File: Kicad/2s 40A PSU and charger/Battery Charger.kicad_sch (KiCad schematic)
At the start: 42 parts

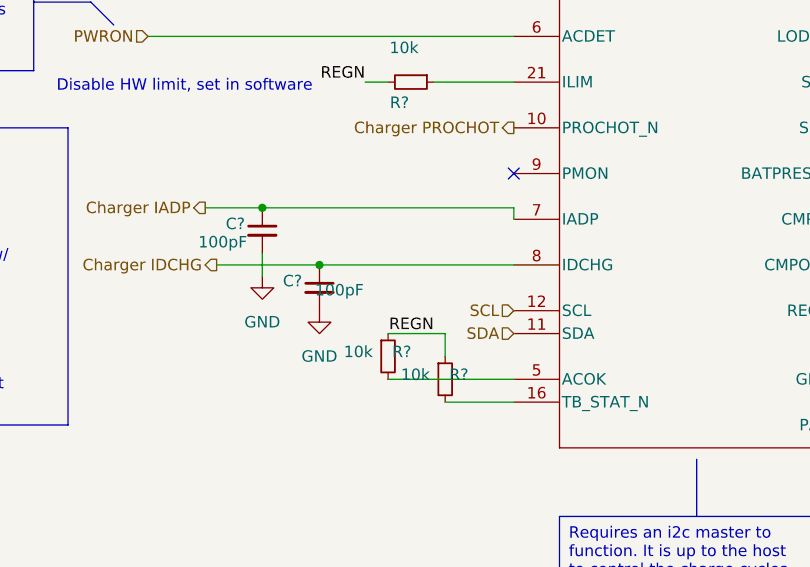
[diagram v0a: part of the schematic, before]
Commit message: Disconnect REGN from unneeded output pullups
These pullups will instead be pulled to 3v3, which should be closer locally. I don't use them but pullups are required for internal detection.
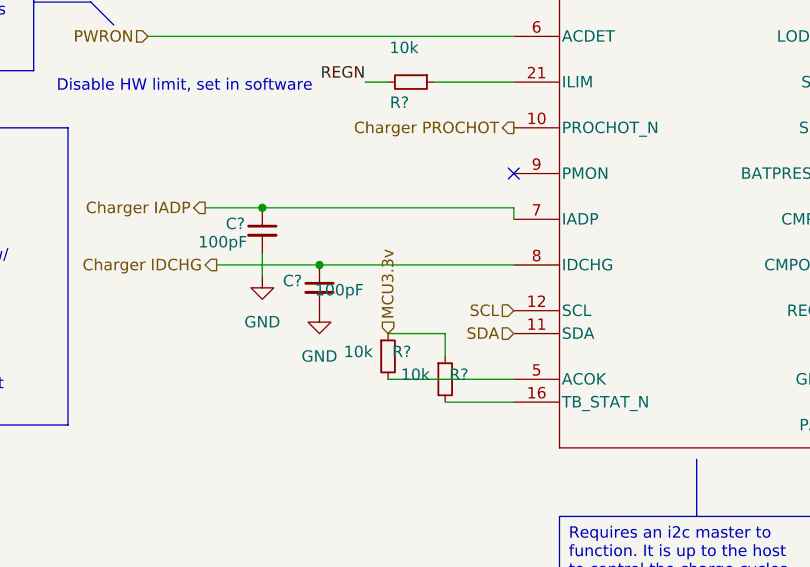
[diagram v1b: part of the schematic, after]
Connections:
- net REGN: no longer R?.1, R?.1
- new net MCU3.3v: R?.1, R?.1
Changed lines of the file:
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@@
-	)
-	(label "REGN"
-		(at 102.87 146.05 180)
-		(fields_autoplaced yes)
-		(effects
-			(font
-				(size 1.27 1.27)
-			)
-			(justify right bottom)
-		)
-		(property "Netclass" "Logic Pwr"
-			(at 102.87 147.32 0)
-			(effects
-				(font
-					(size 1.27 1.27)
-					(italic yes)
-				)
-				(justify right)
-			)
-		)
 	)
 	(label "REGN"
@@
 			(effects
 				(font
+					(size 1.27 1.27)
+					(italic yes)
+				)
+				(justify left)
+			)
+		)
+	)
+	(hierarchical_label "MCU3.3v"
+		(shape input)
+		(at 97.79 146.05 90)
+		(fields_autoplaced yes)
+		(effects
+			(font
+				(size 1.27 1.27)
+			)
+			(justify left)
+		)
+		(property "Netclass" "Logic Pwr"
+			(at 99.06 146.05 90)
+			(effects
+				(font

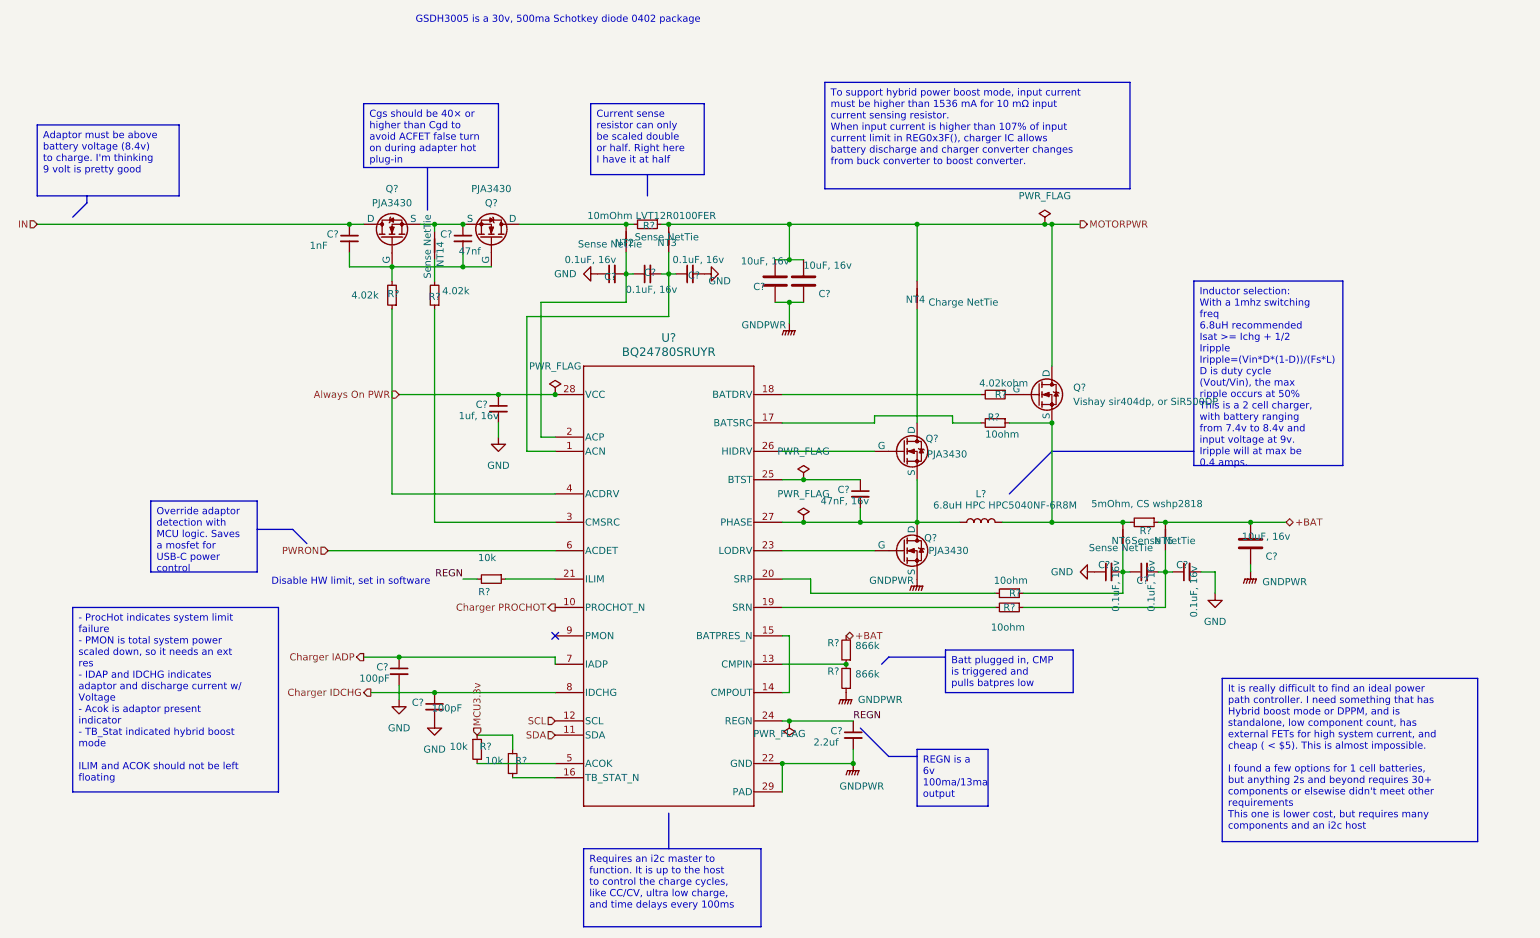
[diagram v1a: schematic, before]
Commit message: Combined separate ground planes
I now have one solid ground plane. There really was no point in having separate ground planes EXCEPT for keeping the high current return path away from the MCU and sense lines. I have added a keepout zone on the top half, to split to keep the high current return from going into the MCU section, but that is it.
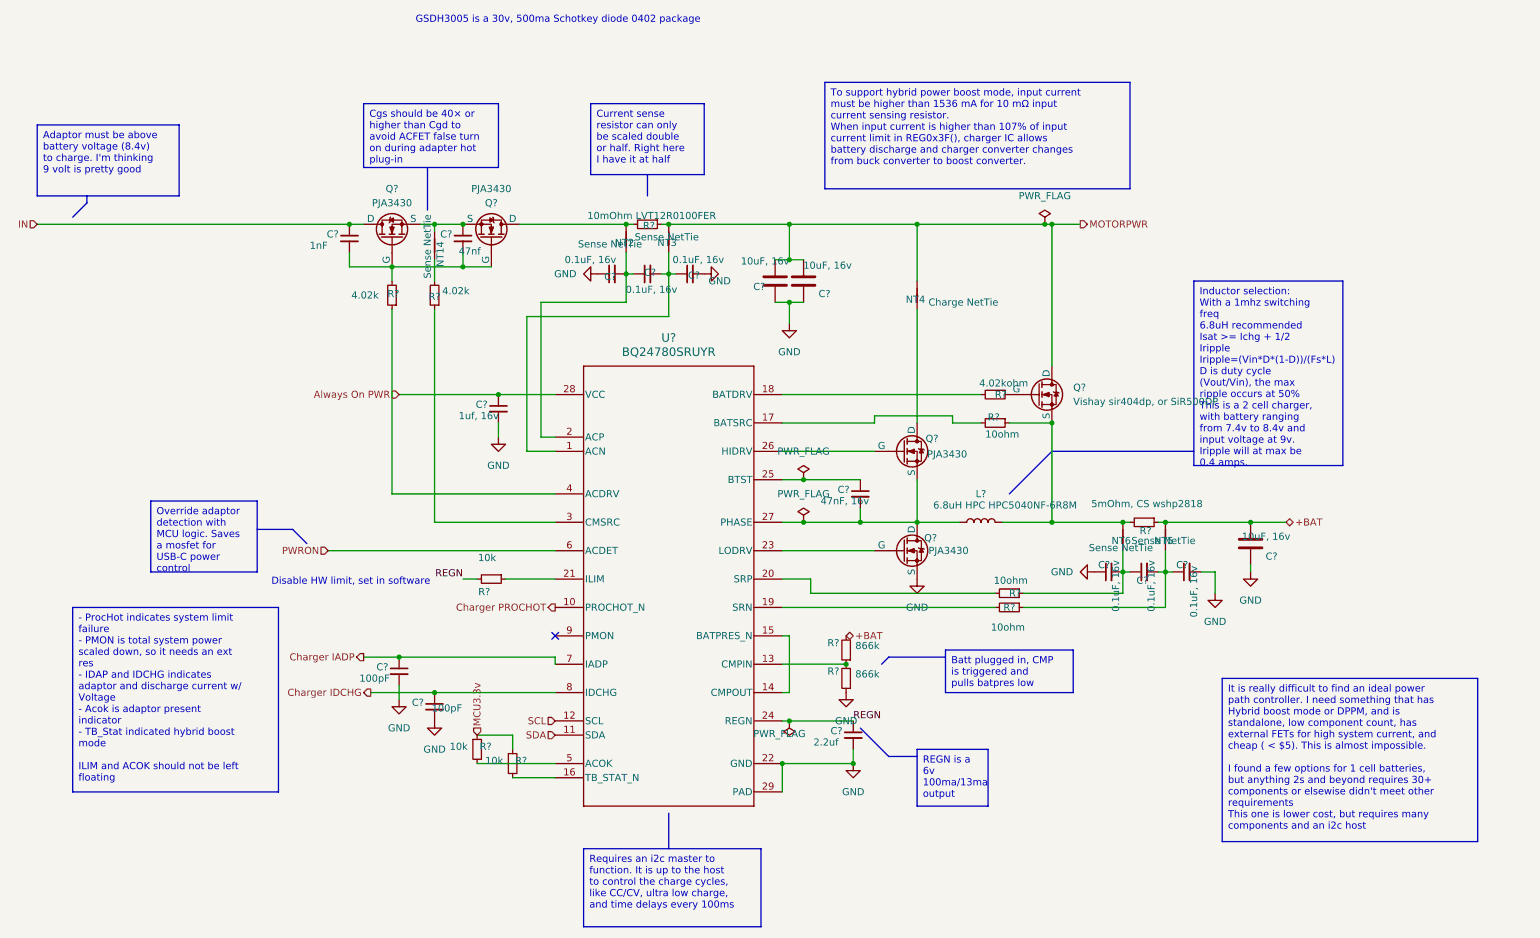
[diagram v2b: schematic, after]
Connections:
- net GNDPWR is gone; now on net GND: C?.1, C?.1, C?.1, C?.2, Q?.3 (S), R?.1, U?.22 (GND), U?.29 (PAD)

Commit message: Fixed incorrect mosfet pin assignments
This was an issue from the last test board I designed that I didn't catch. The mosfets have different pin assignments for drain, gate, and source, and I had messed those up in the schematic by choosing the wrong symbol. This should be fixed now
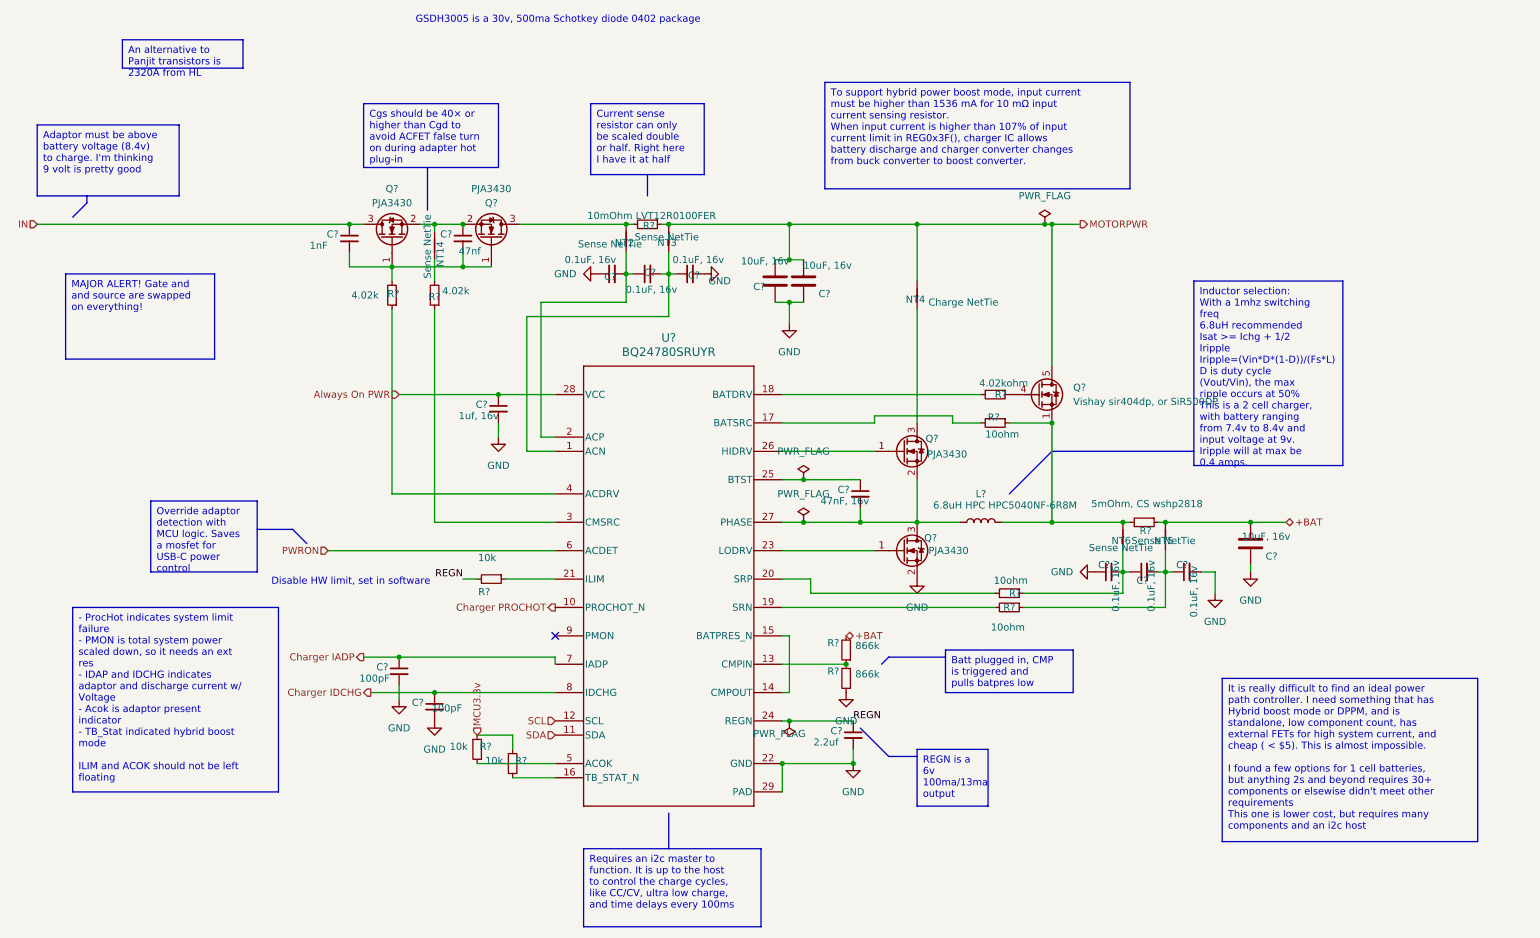
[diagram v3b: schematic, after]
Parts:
- Q? (x4): symbol Simulation_SPICE:NMOS -> Device:Q_NMOS_GSD
- Q?: symbol Simulation_SPICE:NMOS -> custom_Device:Q_NMOS_SGD_8-pin
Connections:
- net GND: now also Q?.2 (S); no longer Q?.3 (S)
- net IN: now also Q?.3 (D); no longer Q?.1 (D)
- net MOTORPWR: now also Q?.5 (D), Q?.6 (D), Q?.7 (D), Q?.8 (D); no longer Q?.1 (D), Q?.2 (D), Q?.3 (D)
- net at C?.2, L?.1, U?.27 (PHASE): now also Q?.2 (S), Q?.3 (D); no longer Q?.1 (D), Q?.3 (S)
- net at U?.23 (LODRV): now also Q?.1 (G); no longer Q?.2 (G)
- net at L?.2, NT6.2, R?.1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: now also Q?.1 (S), Q?.2 (S), Q?.3 (S); no longer Q?.5 (S)
- net at C?.1, NT14.2: now also Q?.2 (S), Q?.2 (S); no longer Q?.3 (S), Q?.3 (S)
- net at C?.2, C?.2, R?.2: now also Q?.1 (G), Q?.1 (G); no longer Q?.2 (G), Q?.2 (G)
- net at NT2.2, R?.2: now also Q?.3 (D); no longer Q?.1 (D)
- net at Q?.1 (G): now also U?.26 (HIDRV); no longer NT4.1
- new net: NT4.1, Q?.3 (D)
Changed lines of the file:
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@@
 		)
 	)
+	(text_box "MAJOR ALERT! Gate and and source are swapped on everything!"
+		(exclude_from_sim no)
+		(at 24.13 63.5 0)
+		(size 26.67 15.24)
+		(stroke
+			(width 0)
+			(type default)
+		)
+		(fill
+			(type none)
+		)
+		(effects
+			(font
+				(size 1.27 1.27)
+			)
+			(justify left top)
+		)
+	)
 	(text_box "REGN is a 6v 100ma/13ma output"
 		(exclude_from_sim no)
@@
 		)
 	)
+	(text_box "An alternative to Panjit transistors is 2320A from HL"
+		(exclude_from_sim no)
+		(at 34.29 21.59 0)
+		(size 21.59 5.08)
+		(stroke
+			(width 0)
+			(type default)
+		)
+		(fill
+			(type none)
+		)
+		(effects
+			(font
+				(size 1.27 1.27)
+			)
+			(justify left top)
+		)
+	)
 	(text_box "- ProcHot indicates system limit failure\n- PMON is total system power scaled down, so it needs an ext res\n- IDAP and IDCHG indicates adaptor and discharge current w/ Voltage\n- Acok is adaptor present indicator\n- TB_Stat indicated hybrid boost mode\n\nILIM and ACOK should not be left floating "
 		(exclude_from_sim no)
@@
 	)
 	(symbol
-		(lib_id "Simulation_SPICE:NMOS")
+		(lib_id "Device:Q_NMOS_GSD")
 		(at 173.99 113.03 0)
 		(unit 1)
@@
 			)
 		)
-		(property "Datasheet" "https://ngspice.sourceforge.io/docs/ngspice-html-manual/manual.xhtml#cha_MOSFETs"
-			(at 173.99 125.73 0)
+		(property "Datasheet" "~"
+			(at 173.99 113.03 0)
 			(effects
 				(font
@@
 			)
 		)
-		(property "Description" "N-MOSFET transistor, drain/source/gate"
+		(property "Description" "N-MOSFET transistor, gate/source/drain"
 			(at 173.99 113.03 0)
 			(effects
@@
 	)
 	(symbol
-		(lib_name "NMOS_1")
-		(lib_id "Simulation_SPICE:NMOS")
+		(lib_id "custom_Device:Q_NMOS_SGD_8-pin")
 		(at 198.12 85.09 0)
 		(unit 1)
@@
 			)
 		)
-		(property "Datasheet" "https://ngspice.sourceforge.io/docs/ngspice-html-manual/manual.xhtml#cha_MOSFETs"
-			(at 198.12 97.79 0)
+		(property "Datasheet" "~"
+			(at 198.12 85.09 0)
 			(effects
 				(font
@@
 			)
 		)
-		(property "Description" "N-MOSFET transistor, drain/source/gate"
+		(property "Description" "N-MOSFET transistor, source/gate/drain"
 			(at 198.12 85.09 0)
 			(effects
@@
 			)
 		)
-		(property "Sim.Pins" "1=D 2=G 3=S"
+		(property "Sim.Pins" "1,2,3=S 4=G 5,6,7,8=D"
 			(at 198.12 100.33 0)
 			(effects
@@
 		(pin "1"
 		)
+		(pin "2"
+		)
+		(pin "3"
+		)
 		(pin "4"
 		)
-		(pin "5"
+		(pin "7"
 		)
-		(pin "2"
+		(pin "8"
 		)
-		(pin "3"
+		(pin "5"
+		)
+		(pin "6"
 		)
 		(instances
@@
 	)
 	(symbol
-		(lib_id "Simulation_SPICE:NMOS")
+		(lib_id "Device:Q_NMOS_GSD")
 		(at 173.99 95.25 0)
 		(unit 1)
@@
 			)
 		)
-		(property "Datasheet" "https://ngspice.sourceforge.io/docs/ngspice-html-manual/manual.xhtml#cha_MOSFETs"
-			(at 173.99 107.95 0)
+		(property "Datasheet" "~"
+			(at 173.99 95.25 0)
 			(effects
 				(font
@@
 			)
 		)
-		(property "Description" "N-MOSFET transistor, drain/source/gate"
+		(property "Description" "N-MOSFET transistor, gate/source/drain"
 			(at 173.99 95.25 0)
 			(effects
@@
 	)
 	(symbol
-		(lib_id "Simulation_SPICE:NMOS")
+		(lib_id "Device:Q_NMOS_GSD")
 		(at 100.33 57.15 270)
 		(mirror x)
@@
 			)
 		)
-		(property "Datasheet" "https://ngspice.sourceforge.io/docs/ngspice-html-manual/manual.xhtml#cha_MOSFETs"
-			(at 87.63 57.15 0)
+		(property "Datasheet" "~"
+			(at 100.33 57.15 0)
 			(effects
 				(font
@@
 			)
 		)
-		(property "Description" "N-MOSFET transistor, drain/source/gate"
+		(property "Description" "N-MOSFET transistor, gate/source/drain"
 			(at 100.33 57.15 0)
 			(effects
@@
 	)
 	(symbol
-		(lib_id "Simulation_SPICE:NMOS")
+		(lib_id "Device:Q_NMOS_GSD")
 		(at 82.55 57.15 90)
 		(unit 1)
@@
 			)
 		)
-		(property "Datasheet" "https://ngspice.sourceforge.io/docs/ngspice-html-manual/manual.xhtml#cha_MOSFETs"
-			(at 95.25 57.15 0)
+		(property "Datasheet" "~"
+			(at 82.55 57.15 0)
 			(effects
 				(font
@@
 			)
 		)
-		(property "Description" "N-MOSFET transistor, drain/source/gate"
+		(property "Description" "N-MOSFET transistor, gate/source/drain"
 			(at 82.55 57.15 0)
 			(effects
